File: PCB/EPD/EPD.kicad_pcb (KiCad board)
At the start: 2 copper layers, 39 x 26 mm, 63 parts, among them J1 Conn_01x26, J2 Shelly, J3 USB-PROG, J4 BTN1, J6 BTN2, J7 USB-C-Socket-V, J8 PWR, P1 +, P10 2, P11 1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

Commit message: silk
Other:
- board text added: "${CURRENT_DATE}"

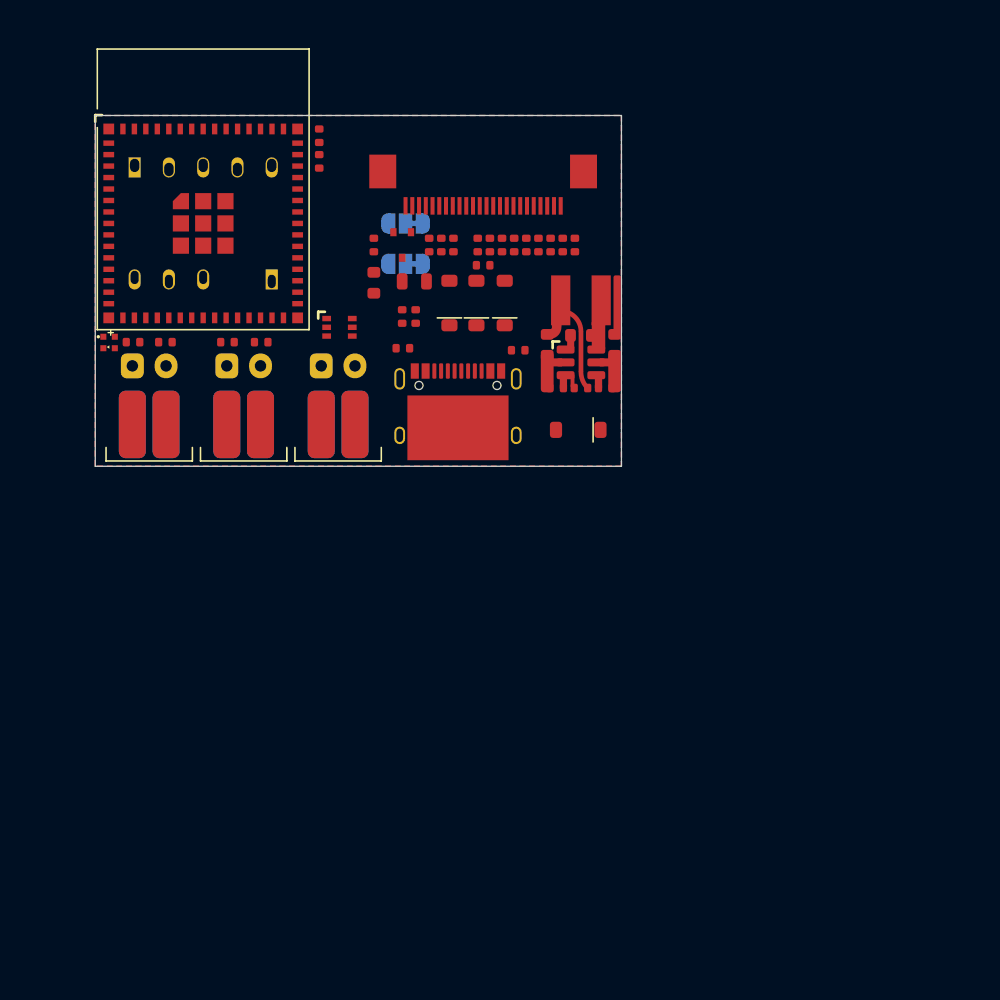
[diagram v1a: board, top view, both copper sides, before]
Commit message: More general EPD driver
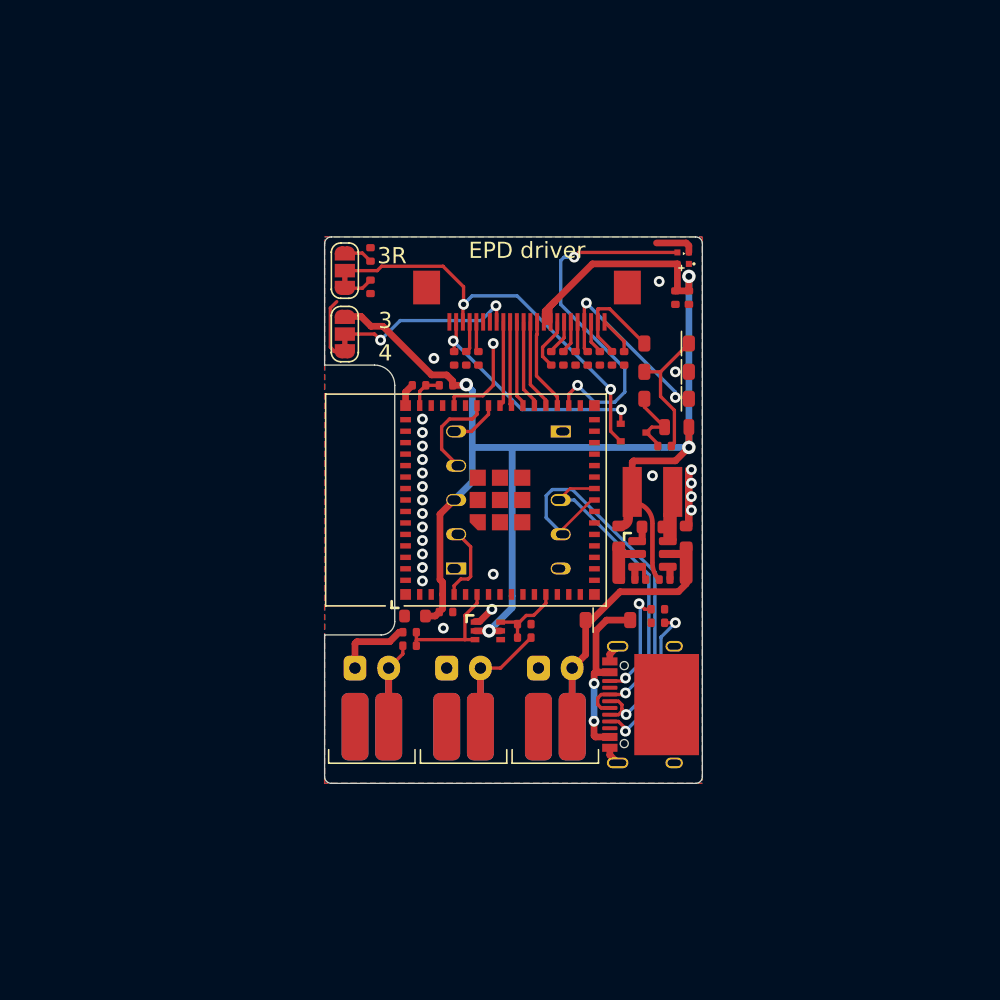
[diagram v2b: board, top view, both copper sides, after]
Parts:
- JP1, JP2: moved to F.Cu
- moved D4 43.0 mm to (112.6, 72.6), turned to 180 degrees
- moved J3 31.1 mm to (103.5, 90.5), turned to 90 degrees
- moved J2 31.0 mm to (95.8, 90.5), turned to -90 degrees
- moved C21 30.3 mm to (100.8, 99.7), turned to 0 degrees
- moved U4 30.1 mm to (99.0, 90.5), turned to 90 degrees
- moved C22 29.7 mm to (92.3, 100.3)
- moved R6 29.3 mm to (100.8, 100.7)
- moved P9 29.2 mm to (97.5, 107.3)
- moved R7 28.9 mm to (92.3, 101.3), turned to 0 degrees
- moved J4 27.8 mm to (89.5, 103.0)
- moved P11 27.8 mm to (90.8, 107.3)
- moved P12 27.8 mm to (88.2, 107.3)
- moved P5 27.8 mm to (90.8, 107.3)
- moved P6 27.8 mm to (88.2, 107.3)
- moved R4 27.8 mm to (110.7, 99.6)
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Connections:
- U4 pad 12: unconnected-(U4-GPIO8-Pad12) -> BTN2
- U4 pad 29: RGB -> unconnected-(U4-GPIO34-Pad29)
- U4 pad 31: BUSY -> unconnected-(U4-GPIO35-Pad31)
- U4 pad 32: RST -> RGB
- U4 pad 33: DC -> MOSI
- U4 pad 34: CS -> CLK
- U4 pad 35: CLK -> CS
- U4 pad 36: MOSI -> DC
- U4 pad 37: BTN1 -> RST
- U4 pad 38: BTN2 -> BUSY
- U4 pad 6: unconnected-(U4-GPIO2-Pad6) -> BTN1
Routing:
- net +3.3V: track 0.00 -> 101.9 mm, vias 0 -> 4
- net D-: track 0.00 -> 32.0 mm, vias 0 -> 1
- net GND: track 0.00 -> 30.4 mm, vias 0 -> 25
- net Net-(J1-Pin_3): track 0.00 -> 30.4 mm, vias 0 -> 2
- net RGB: track 0.00 -> 26.7 mm, vias 0 -> 2
- net D+: track 0.00 -> 25.2 mm, vias 0 -> 1
- net PWR: track 0.00 -> 22.7 mm
- net Net-(J1-Pin_2): track 0.00 -> 18.0 mm, vias 0 -> 2
- net Net-(D2-K): track 0.00 -> 14.4 mm, vias 0 -> 2
- net Net-(D6-A): track 0.00 -> 14.0 mm, vias 0 -> 2
- net Net-(J1-Pin_8): track 0.00 -> 13.7 mm, vias 0 -> 2
- net Net-(J6-Pin_2): track 0.00 -> 13.4 mm
- net Net-(J7-CC1): track 0.00 -> 11.9 mm, vias 0 -> 2
- net Net-(J4-Pin_2): track 0.00 -> 10.8 mm
- net Net-(D1-K): track 0.00 -> 10.2 mm
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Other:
- board size 39 x 26 mm -> 28 x 40.5 mm
- board text added: "1"
- board text added: "2"
- board text added: "39"
- board text added: "8"
- board text added: "A"
- board text added: "EPD driver"
- board text added: "www.me.uk"
- board text removed: "0R47"
- board text removed: "34"
- board text removed: "35"
- board text removed: "SPI"

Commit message: Panel
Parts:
- added PCB1: 70x70, RevK:PCB7070, F.Cu at (99.0, 90.5)
- added V1: ~, RevK:VCUT70N, F.Cu at (114.0, 90.5)
- added V3: ~, RevK:VCUT70N, B.Cu at (86.0, 90.5)
- added V4: ~, RevK:VCUT70N, F.Cu at (99.0, 111.5)
- added V6: ~, RevK:VCUT70N, B.Cu at (99.0, 71.0)
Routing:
- net GND: track 30.4 -> 35.5 mm, vias 25 -> 26
- net Net-(D2-A): track 5.44 -> 6.64 mm
- net +3.3V: track 101.9 -> 102.8 mm
- net Net-(D6-A): track 14.0 -> 13.2 mm
- net Net-(D1-A): track 8.04 -> 7.38 mm
- net D+: track 25.2 -> 24.5 mm
- net Net-(JP2-B): track 2.15 -> 1.60 mm
- net Net-(JP2-A): track 2.15 -> 1.60 mm
- net RGB: track 26.7 -> 26.2 mm
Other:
- board size 28 x 40.5 mm -> 70 x 70 mm

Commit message: Product code
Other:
- board text added: "5060634238144"
- board text added: "epd.revk.uk"
- board text removed: "www.me.uk"
